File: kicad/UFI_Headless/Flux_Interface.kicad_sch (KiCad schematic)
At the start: 20 parts, among them J11 WRITE_LOCK, U14 74LVC1G32GW, U6 SN74LS07D, U7 SN74LS07D, U8 74LVC14AD

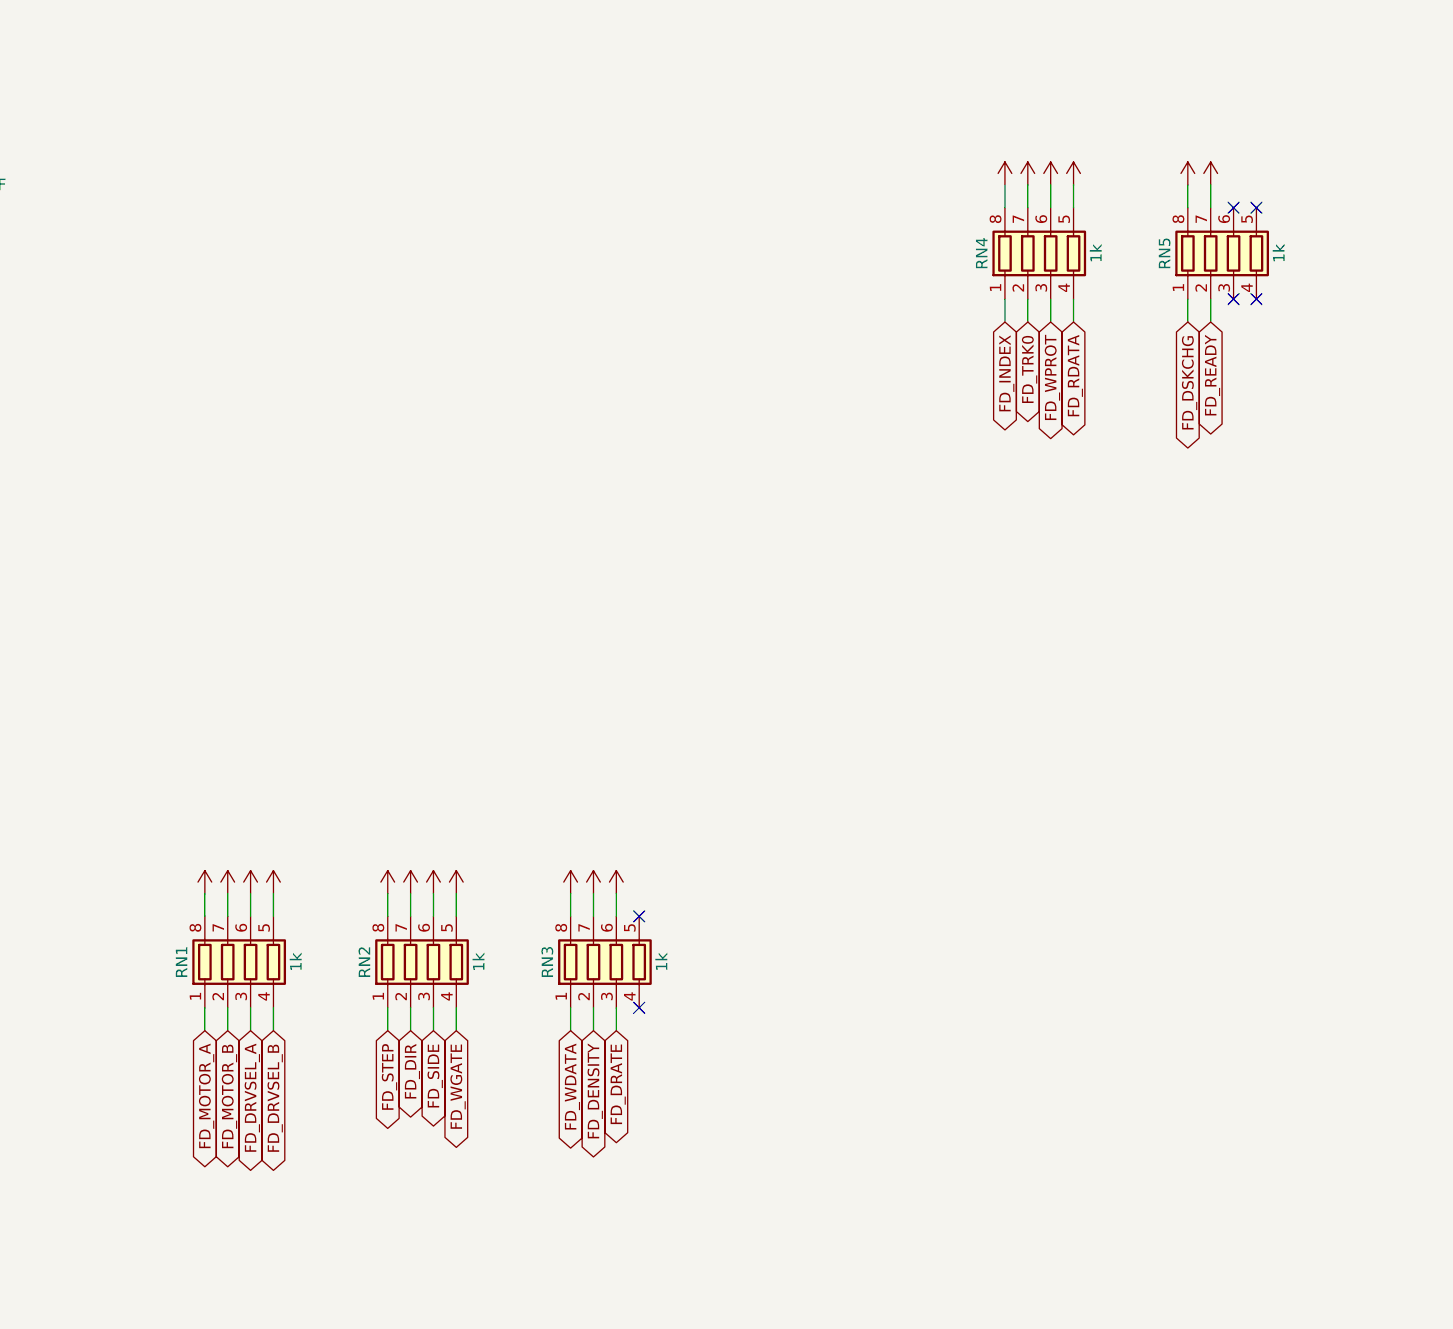
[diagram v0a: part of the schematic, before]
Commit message: KiCad v0.7 rework, schematic stages A1-A3: automatic 5 V source selection, discrete FDD termination, front-panel header - Power: J18 (5V_SEL jumper) removed, U19 TPS2116DRL selects external 5 V (J17, priority) or the 12 V buck automatically (R72 33k / R73 10k PR1 divider, C57 1 uF, status via R74 10k to +3V3 on test point TP9 TP_5V_SEL), PWR_FLAG moved to +5V_PSU_F; Flux_Interface / IEC_Bus / FDD_Connectors: RN1-RN8 (1k R_Pack04) replaced by 25 discrete 0603 1k resistors R75-R99 on the same nets (17 FDD lines, 5 IEC, 3 Amiga), array stubs, per-pin +5V symbols and orphan no-connects removed; MCU_Core: J9 EXPANSION and J13 MODE_SW removed, J12 becomes a keyed 2x8 IDC front-panel header FRONT (1 +3V3, 3 ACT, 5 ERR, 7 USB, 9 FDD, 11 PWR via R34-R37 and new R100 330 R, 13 BTN_A, 14 BTN_B, 15 MODE1, 16 MODE2 via R101-R104 470 R and TVS D18-D21, even pins 2-12 GND), on-board LEDs D5-D8 with R12-R15 removed (D4 ACT stays), SW3/SW4 marked DNP (buttons on the front); lib_symbols for Conn_02x08_Odd_Even and D_TVS added to MCU_Core; ERC over the whole project 0 errors / 0 warnings. Design brief docs/PCB_Revision_Empfehlungen_2026-10-24.md (decisions of 2026-10-24: power as before minus J18, input edge vs. drive edge, DB23 Amiga at the drive edge, W5500 LAN at the input edge, 32x 0603 termination), bring-up procedure docs/Bringup_2026-10-24.md (USB-C J1 soldered rotated 180 deg on the first board). Open for A4/A5: INDEX_SIM needs its own timer-capable MCU pin (PE1 is now the MODE2 line; firmware pin map changes in the same commit as the schematic), I2C SCL/SDA get 4 test pads, D18-D21 to be swapped for low-leakage ESD diodes (SMF3.3CA leaks up to 1 mA at 3.3 V against ~40k internal pull-ups) plus ESD on the five LED lines, +3V3 on J12 pin 1 to be fed through a 1k series resistor, loopback block, LA header, J11 slide switch, DIN-6 and DB23, W5500, then layout (USB-C edge cutout, input/output edges). Layout (.kicad_pcb) not yet touched.
Claude-Session: https://claude.ai/code/sessi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
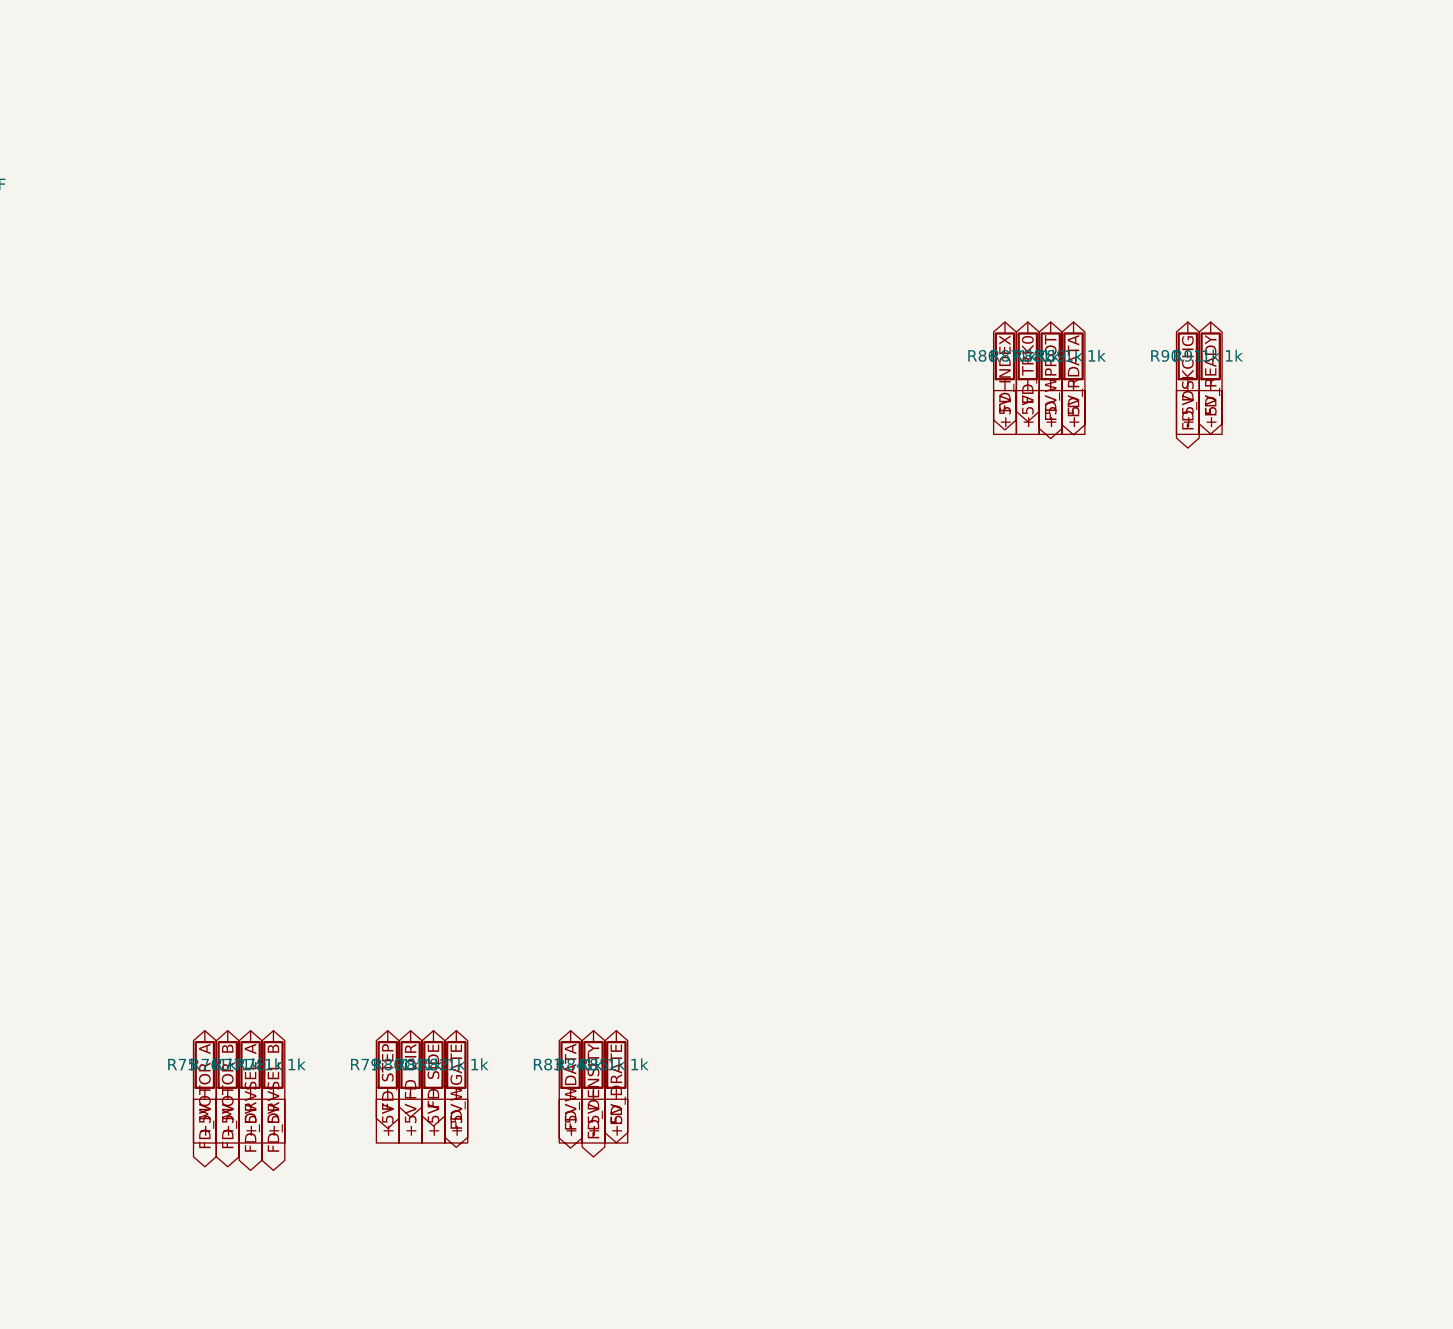
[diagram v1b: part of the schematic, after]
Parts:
- removed RN1, RN2, RN3, RN4, RN5: 1k, Resistor_SMD:R_Array_Convex_4x0603, symbol Device:R_Pack04
- added R75, R76, R77, R78, R79, R80, R81, R82, R83, R84, R85, R86, R87, R88, R89, R90, R91: 1k, Resistor_SMD:R_0603_1608Metric, symbol Device:R
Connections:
- net +5V: now also R75.2, R76.2, R77.2, R78.2, R79.2, R80.2, R81.2, R82.2, R83.2, R84.2, R85.2, R86.2, R87.2, R88.2, R89.2, R90.2, R91.2
- net FD_DENSITY: now also R84.1
- net FD_DIR: now also R80.1
- net FD_DRATE: now also R85.1
- net FD_DRVSEL_A: now also R77.1
- net FD_DRVSEL_B: now also R78.1
- net FD_DSKCHG: now also R90.1
- net FD_INDEX: now also R86.1
- net FD_MOTOR_A: now also R75.1
- net FD_MOTOR_B: now also R76.1
- net FD_RDATA: now also R89.1
- net FD_READY: now also R91.1
- net FD_SIDE: now also R81.1
- net FD_STEP: now also R79.1
- net FD_TRK0: now also R87.1
- net FD_WDATA: now also R83.1
- net FD_WGATE: now also R82.1
- net FD_WPROT: now also R88.1
- no-connect marks 7 -> 1

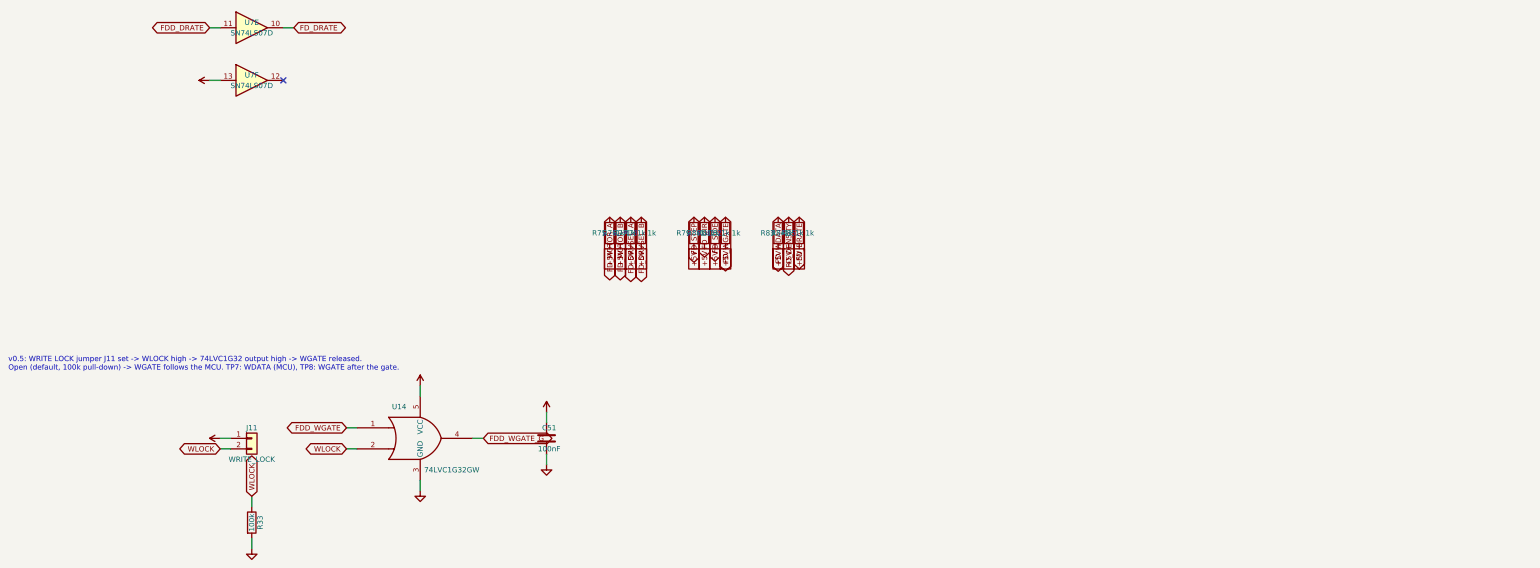
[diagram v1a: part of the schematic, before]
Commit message: KiCad v0.7 rework, schematic stage A4 with the matching firmware pin map: electronic self-test loopback, index simulation on its own timer pin, PSU-guard header, LA header - owner's constraint of 2026-10-24: the board sits in a closed enclosure, only LAN and USB stay reachable, nothing is pluggable after assembly, so no jumpers or slide switches for operation. Flux_Interface: J11 WRITE_LOCK pin header replaced by solder jumper JP4 (+3V3 to WLOCK, R33 100k pull-down and the U14 LVC1G32 hardware gate unchanged); INDEX_SIM is a global net from PE5 (TIM15_CH1, verified against the ST pin database via the embassy stm32h723zg tables) through the until now unused open-collector buffer U7F (pin 13 was tied to +5V) onto FD_INDEX, wired-OR like the J19 sync sensor, so the self-test index loop needs no wire; new loopback block U22 TS5A3166DBVR (SOT-23-5, pins 1 NO = FD_RDATA, 2 COM = FD_WDATA, 3 GND, 4 IN = LOOP_EN, 5 V+ = +5V; TI datasheet: V+ 1.65-5.5 V, VIH 2.4 V at 5 V, control input 0-5.5 V), C58 100n, R106 100k pull-down on LOOP_EN (open during reset), Q5 2N7002 pulls FD_TRK0 low with LOOP_EN; note text updated. IEC_Bus: the spare inverter U10F (input was GND, output no-connect) reads FD_WGATE back as WGATE_SENSE. MCU_Core: U5 PE5 INDEX_SIM, PG14 LOOP_EN, PG15 WGATE_SENSE, PG7 GUARD_OFF, PG8 GUARD_ERR5, PG13 GUARD_ERR12 (six no-connect flags removed); J20 GUARD 1x4 (1 GND, 2 OFF, 3 ERR5, 4 ERR12 with R107/R108 10k pull-ups) for the C64 PSU Guard board's J3; J21 LA 2x10 logic-analyser header on the 3.3 V side (1 RDATA, 3 WDATA, 5 INDEX, 7 WGATE, 9 STEP, 11 DIR, 13 SIDE, 15 DRVSEL_A, 17 MOTOR_A, 19 TRK0, 2 WPROT, 4 DSKCHG, 6 READY, 8 DENSITY, 10 INDEX_SIM, 12 LOOP_EN, 14 WGATE_SENSE, 16/18/20 GND); lib symbols TS5A3166DBVR, 2N7002, SolderJumper_2_Open, Conn_01x04, Conn_02x10_Odd_Even added to the sheets. ERC over the whole project 0 errors / 0 warnings. Firmware (same commit, as agreed): board.h/board_headless.c pin table PIN_INDEX_SIM PE5 (INDEX_SIM_AF = AF4), PIN_LOOP_EN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
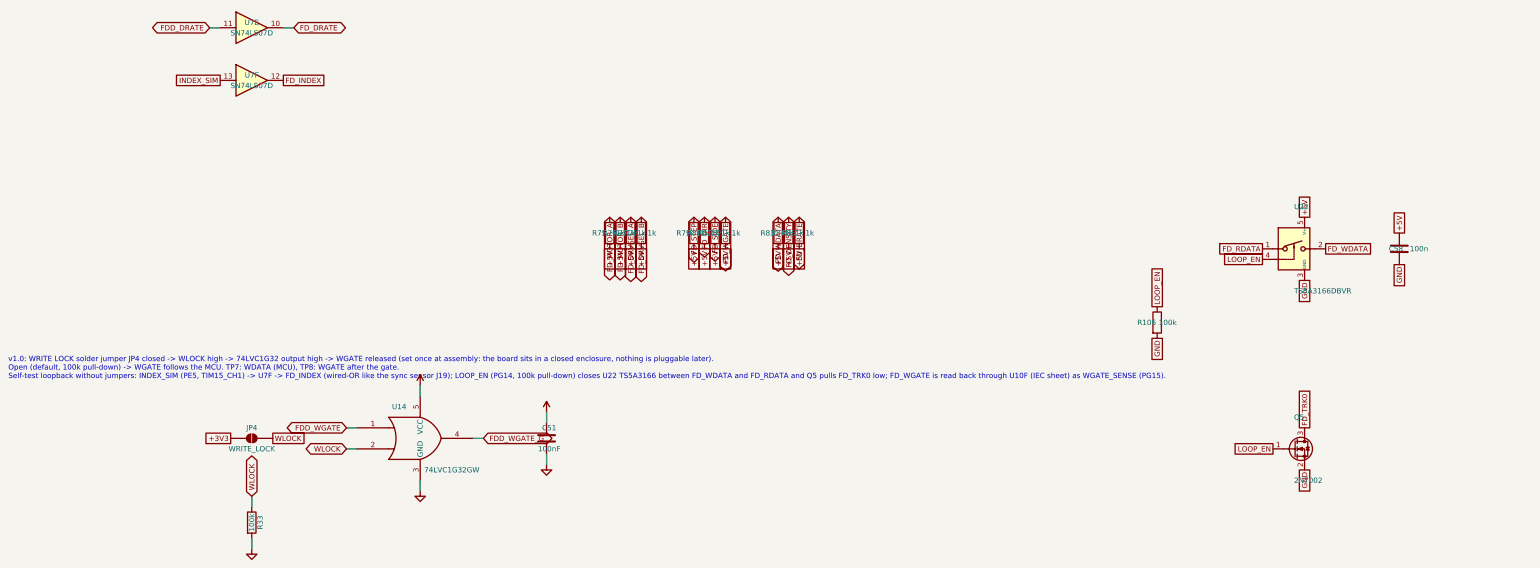
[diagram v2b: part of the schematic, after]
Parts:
- removed J11: WRITE_LOCK, Connector_PinHeader_2.54mm:PinHeader_1x02_P2.54mm_Vertical, symbol Connector_Generic:Conn_01x02
- added C58: 100n, Capacitor_SMD:C_0603_1608Metric, symbol Device:C
- added JP4: WRITE_LOCK, Jumper:SolderJumper-2_P1.3mm_Open_RoundedPad1.0x1.5mm, symbol Jumper:SolderJumper_2_Open
- added Q5: 2N7002, Package_TO_SOT_SMD:SOT-23, symbol Transistor_FET:2N7002
- added R106: 100k, Resistor_SMD:R_0603_1608Metric, symbol Device:R
- added U22: TS5A3166DBVR, Package_TO_SOT_SMD:SOT-23-5, symbol Analog_Switch:TS5A3166DBVR
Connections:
- net +3V3: now also JP4.1 (A)
- net +5V: now also C58.1, U22.5 (V+); no longer U7.13
- net FD_INDEX: now also U7.12
- net FD_RDATA: now also U22.1
- net FD_TRK0: now also Q5.3 (D)
- net FD_WDATA: now also U22.2
- net GND: now also C58.2, Q5.2 (S), R106.2, U22.3 (GND)
- net WLOCK: now also JP4.2 (B)
- new net INDEX_SIM: U7.13
- new net LOOP_EN: Q5.1 (G), R106.1, U22.4
- no-connect marks 1 -> 0
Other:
- note added: "v1.0: WRITE LOCK solder jumper JP4 closed -> WLOCK high -> 74LVC1G32 output high -> WGATE released (set once at assembly: the board sits in a closed enclosure, nothing is pluggable later). Open (default, 100k pull-down) -> WGATE follows the MCU. TP7: WDATA (MCU), TP8: WGATE after the gate. Self-test loopback without jumpers: INDEX_SIM (PE5, TIM15_CH1) -> U7F -> FD_INDEX (wired-OR like the sync se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"
- note removed: "v0.5: WRITE LOCK jumper J11 set -> WLOCK high -> 74LVC1G32 output high -> WGATE released. Open (default, 100k pull-down) -> WGATE follows the MCU. TP7: WDATA (MCU), TP8: WGATE after the gate."

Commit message: KiCad v0.7 rework, stage B2: board v1.0 placed and routed, DRC 0 errors / 0 warnings / 0 unconnected with schematic parity - J1 USB-C and J22 RJ45 turned so that their openings cross the input edge (rot 180 at y 2.66 / 13.11 mm; at rotation 0 both library footprints open towards the board, which is how the USB-C receptacle stood since v0.1), DRU rule idc_edge_silk extended to J1/J22/J12 (silk over the edge is clipped by the fab, justified in the file), old J9 spoke rule removed; final placement by scripts/eco/place_v10.py plus relayout_lan.py (Y2/C59/C60/R109 crystal cluster and the 3V3A filter re-laid under U23, SW3 DNP parked on B.Cu under J22 pending the owner's SW3/SW4 decision); routing: the make_pcb.sh pipeline (Freerouting 2.4.1) hit the 1800 s timeout and left 154 connections open at the 0.5-mm QFP rows of U5/U23, so the rest was done with new ECO tools - rip_net.py (corridors), fanout.py (0.5/0.25 mm dogbone vias in two rows), shrink_vias.py, batch_route.py (A* over the kicad-cli DRC JSON: every grid step checked as a segment, string-pulling per layer run, via cost in mm, start at fan-out vias, ROUTE_CLR/ROUTE_W overrides), add_vias.py (GND stitches for isolated GND pads U23.29, C29.2, U13.2/C50.2), drop_pours.py + power_pours.py (stale supply pours had bridged five missing +5V tracks at R92-R96), trim_dangling.py, hide_small_refs.py (references only for ICs, connectors, switches, crystals, fuses, inductors, D4), place_silk.py (references/texts to the nearest free silk spot, F and B); schematic: TP9-TP13 and JP4 in_bom no (set_in_bom.py), footprint Description fields synced from the symbols (netlist.py/sync_fields.py) so the parity check is clean; picture docs/layout_v1.0_2026-10-24.png; PLAN.md B2 done, kicad README layout v1.0 section, scripts/eco/README.md. Owner skill pcb-routing (installed today) applied: routing_rules.json with the 16 load nets (F1/F4 1.5 A, F2/F3 1.1 A with cut-off above 1.5 A, buck 2 A) and 24 load paths, net class Load 1.0 mm / 0.8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
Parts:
- JP4, U6: now left out of the parts list
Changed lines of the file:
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@@
 		(unit 1)
 		(exclude_from_sim no)
-		(in_bom yes)
+		(in_bom no)
 		(on_board yes)
 		(dnp no)
@@
 		(unit 1)
 		(exclude_from_sim no)
-		(in_bom yes)
+		(in_bom no)
 		(on_board yes)
 		(dnp no)
